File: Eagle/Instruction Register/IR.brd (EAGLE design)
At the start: 160 x 100 mm, 55 parts, among them IC1 SN74HC04N, IC2 SN74HC04N, IC3 SN74HC04N, J1 55959-1630

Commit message: added parts needed to finish boards
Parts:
- added J2: 55959-2430, SamacSys_Parts:559592430
- J1: value 55959-1630 -> 55959-2030; device SamacSys_Parts:SHDR16W65P250X200_2X8_1940X140 -> SamacSys_Parts:55959-2030_1
- moved J1 100.7 mm to (-115.6, -10.2)

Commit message: Finished IR
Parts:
- removed IC3: SN74HC04N, SamacSys_Parts:DIP794W53P254L1930H508Q14N
- moved IC1 244.9 mm to (149.9, 64.8)
- moved CLOCK_GATE 240.9 mm to (110.5, 68.6)
- moved J2 240.0 mm to (80.0, 90.2)
- moved IC2 238.7 mm to (132.1, 64.8)
- moved J1 207.6 mm to (61.0, 99.1)
- moved LEDHLT 186.4 mm to (58.4, 11.4), turned to 270 degrees
- moved RHLT 184.5 mm to (58.4, 20.3), turned to 90 degrees
- moved CONTROL_LOGIC_0-7 181.9 mm to (138.4, 40.6), turned to 90 degrees
- moved CONTROL_LOGIC_16-23 125.5 mm to (64.8, 40.6), turned to 90 degrees
- moved MICROCODE_COUNTER 124.9 mm to (74.9, 67.3)
- moved CONTROL_LOGIC_8-15 124.9 mm to (101.6, 40.6), turned to 90 degrees
- moved IR_OUT_0-7 99.2 mm to (34.3, 80.0)
- moved IR_OUT_8-15 94.4 mm to (16.5, 80.0)
- moved ONE_0-7 89.7 mm to (35.6, 10.2), turned to 90 degrees
- moved ONE_8-15 89.1 mm to (35.6, 22.9), turned to 90 degrees
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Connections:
- removed net N$25: CONTROL_LOGIC_0-7.9
- removed net N$26: CONTROL_LOGIC_0-7.10
- removed net N$27: CONTROL_LOGIC_0-7.11
- removed net N$28: CONTROL_LOGIC_0-7.13
- new net C0: CONTROL_LOGIC_0-7.9, J2.1
- new net C1: CONTROL_LOGIC_0-7.10, J2.3
- new net C2: CONTROL_LOGIC_0-7.11, J2.5
- new net C3: CONTROL_LOGIC_0-7.13, J2.7
- net !ACO: now also J2.11
- net !ALUO: now also J2.15
- net !CO: now also J2.19
- net !IRO: now also J2.14
- net !JMP: now also J2.23
- net !MBRO: now also J2.4
- net !MCR: now also J2.20, MICROCODE_COUNTER.1
- net !ONE: now also J2.12
- net !RI: now also J2.8
- net !RO: now also J2.10
- net !SC: now also J2.9
- net ACI: now also J2.13
- net CE: now also J2.21
- net CLK: now also J1.18
- net GND: now also CLOCK_GATE.10, CLOCK_GATE.12, CLOCK_GATE.13, CLOCK_GATE.4, CLOCK_GATE.5, CLOCK_GATE.9, J1.20
- net HLT: now also J2.24
- net INPUT: now also J2.18
- net IRI: now also J2.16
- net MARI: now also J2.6
- net MBRI: now also J2.2
- net OI: now also J2.22
- net RST: now also J1.17
- net SU: now also J2.17
- net VCC: now also J1.19

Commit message: finished most boards
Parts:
- added C1, C2, C3, C4: (no value), rcl:C025-024X044
- added LED0, LED1, LED10, LED11, LED2, LED3, LED4, LED5, LED6, LED7, LED8, LED9: YELLOW, led:LED3MM
- added LED13, LED14, LED15, LEDACO: BLUE, led:LED3MM
- added R0, R1, R10, R11, R13, R14, R15, R2, R3, R4, R5, R6, R7, R8, R9, RACO: 220, rcl:0204/7
- added U$1, U$2, U$3, U$4: (no value), holes:2,8
- moved LED12 109.2 mm to (24.1, 64.8), turned to 90 degrees
- moved R12 101.7 mm to (24.1, 55.9), turned to 270 degrees
- moved IR_8-15 24.3 mm to (38.1, 49.5), turned to 90 degrees
- moved IR_OUT_0-7 22.9 mm to (57.1, 78.7), turned to 90 degrees
- moved MICROCODE_COUNTER 21.6 mm to (96.5, 68.6)
- moved LEDCE 5.68 mm to (129.5, 14.0)
- moved LEDOI 5.68 mm to (83.8, 14.0)
- moved LEDRI 5.68 mm to (144.8, 14.0)
- moved LEDRO 5.68 mm to (139.7, 14.0)
- moved RCE 5.68 mm to (129.5, 22.9)
- moved ROI 5.68 mm to (83.8, 22.9)
- moved RRI 5.68 mm to (144.8, 22.9)
- moved RRO 5.68 mm to (139.7, 22.9)
- moved LEDACI 5.68 mm to (119.4, 14.0)
- moved LEDALUO 5.68 mm to (99.1, 14.0)
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- renumbered IC1 to NOT_GATE_1, IC2 to NOT_GATE_2, J1 to BUS, J2 to CONTROL_LOGIC
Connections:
- new net N$21: LEDACO.A, RACO.1
- new net N$25: LED1.A, R1.1
- new net N$26: LED2.A, R2.1
- new net N$27: LED3.A, R3.1
- new net N$28: LED4.A, R4.1
- new net N$29: LED5.A, R5.1
- new net N$30: LED6.A, R6.1
- new net N$31: LED7.A, R7.1
- new net N$32: LED8.A, R8.1
- new net N$34: LED9.A, R9.1
- new net N$35: LED10.A, R10.1
- new net N$36: LED11.A, R11.1
- new net N$38: LED13.A, R13.1
- new net N$39: LED14.A, R14.1
- new net N$40: LED15.A, R15.1
- new net N$41: LED0.A, R0.1
- new net N$42: LED0.K, LED1.K, LED10.K, LED11.K, LED12.K, LED13.K, LED14.K, LED15.K, LED2.K, LED3.K, LED4.K, LED5.K, LED6.K, LED7.K, LED8.K, LED9.K
- net ACO: now also RACO.2; no longer R12.2
- net GND: now also C1.1, C2.1, C3.1, C4.1, LEDACO.K; no longer LED12.K
- net IR0: now also R0.2
- net IR1: now also R1.2
- net IR10: now also R10.2
- net IR11: now also R11.2
- net IR12: now also R12.2
- net IR13: now also R13.2
- net IR14: now also R14.2
- net IR15: now also R15.2
- net IR2: now also R2.2
- net IR3: now also R3.2
- net IR4: now also R4.2
- net IR5: now also R5.2
- net IR6: now also R6.2
- net IR7: now also R7.2
- net IR8: now also R8.2
- net IR9: now also R9.2
- net VCC: now also C1.2, C2.2, C3.2, C4.2
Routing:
- net GND: track 0.00 -> 633.3 mm, vias 0 -> 1
- net VCC: track 0.00 -> 472.5 mm, vias 0 -> 4
- net !ONE: track 0.00 -> 246.0 mm, vias 0 -> 1
- net IR14: track 0.00 -> 211.5 mm, vias 0 -> 3
- net IR13: track 0.00 -> 201.1 mm, vias 0 -> 2
- net B10: track 0.00 -> 200.9 mm, vias 0 -> 2
- net B5: track 0.00 -> 197.9 mm
- net INPUT: track 0.00 -> 193.4 mm, vias 0 -> 2
- net IR15: track 0.00 -> 190.8 mm, vias 0 -> 4
- net CE: track 0.00 -> 180.7 mm
- net !IRO: track 0.00 -> 173.8 mm, vias 0 -> 4
- net B4: track 0.00 -> 172.3 mm
- net MARI: track 0.00 -> 161.3 mm, vias 0 -> 2
- net IRI: track 0.00 -> 161.3 mm, vias 0 -> 2
- net IR12: track 0.00 -> 160.3 mm, vias 0 -> 5
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
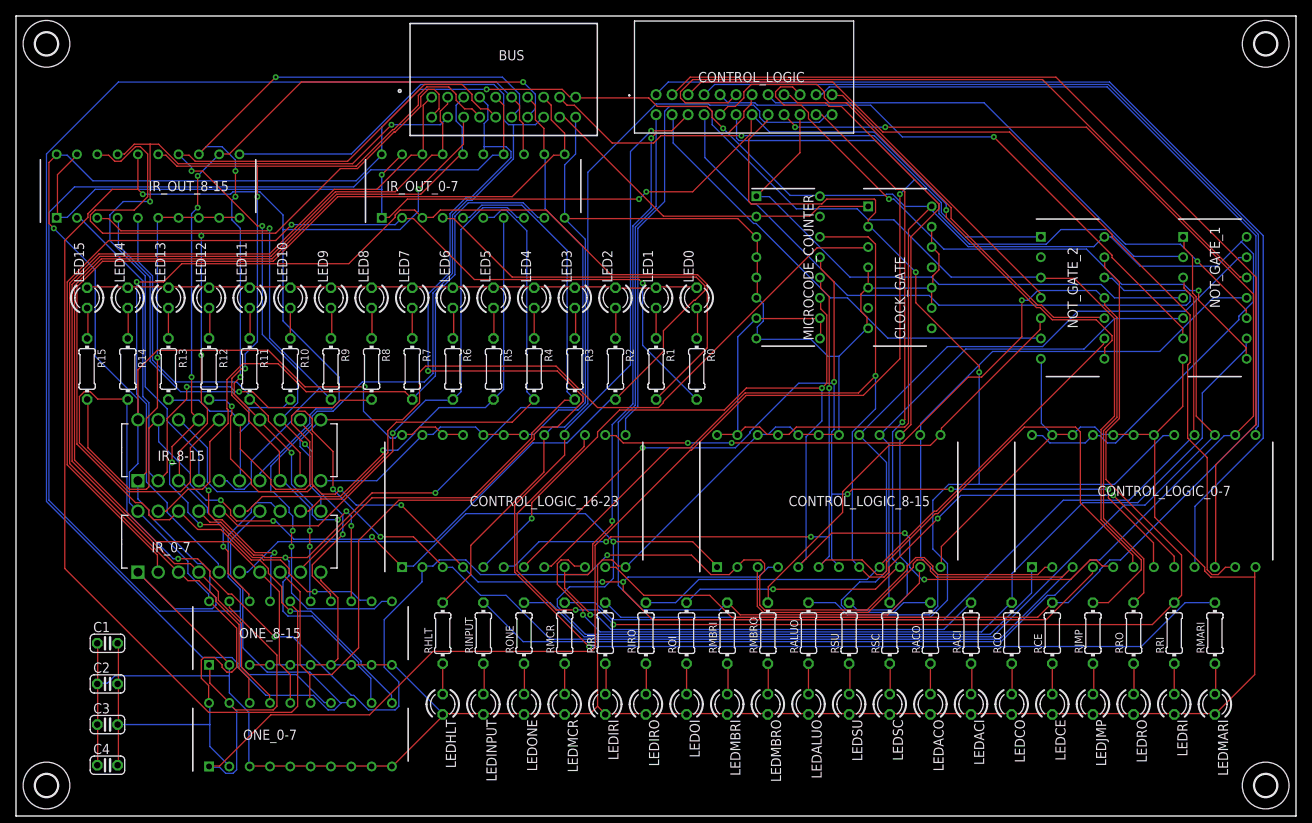
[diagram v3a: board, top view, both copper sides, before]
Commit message: added Clock
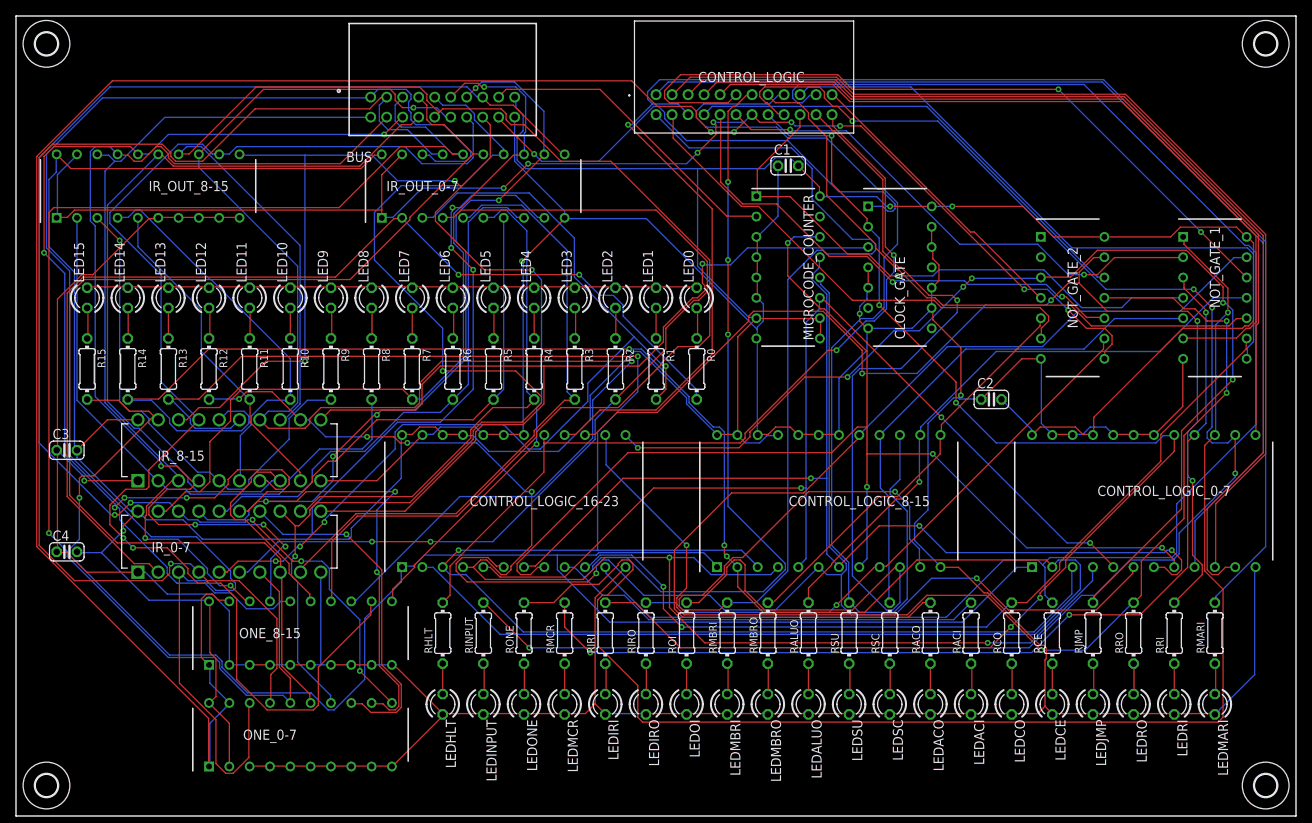
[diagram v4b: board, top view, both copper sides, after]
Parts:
- moved C2 116.1 mm to (121.9, 52.1)
- moved C1 103.9 mm to (96.5, 81.3)
- moved C3 34.7 mm to (6.35, 45.7)
- moved C4 27.1 mm to (6.35, 33.0)
- moved BUS 7.62 mm to (53.3, 99.1)
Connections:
- new net !CLK: BUS.17, MICROCODE_COUNTER.2
- net CLK: no longer MICROCODE_COUNTER.2
- net RST: no longer BUS.17
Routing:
- net B12: track 116.1 -> 200.0 mm, vias 4 -> 0
- net B5: track 197.9 -> 126.8 mm, vias 0 -> 5
- net RST: track 68.9 -> 0.00 mm, vias 1 -> 0
- net B0: track 121.2 -> 182.8 mm
- net B13: track 119.8 -> 181.0 mm, vias 8 -> 2
- net ONE: track 125.1 -> 177.8 mm, vias 0 -> 1
- net IR14: track 211.5 -> 263.9 mm
- net B10: track 200.9 -> 154.2 mm, vias 2 -> 5
- net SU: track 84.9 -> 127.7 mm
- net MBRI: track 104.5 -> 146.9 mm, vias 0 -> 1
- net B14: track 124.1 -> 164.1 mm, vias 7 -> 2
- net MARI: track 161.3 -> 200.7 mm, vias 2 -> 1
- net !CLK: track 0.00 -> 39.2 mm
- net B4: track 172.3 -> 134.6 mm, vias 0 -> 2
- net B2: track 132.0 -> 166.9 mm, vias 0 -> 1
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
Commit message: added gerber files for each board
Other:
- board text added: "MARIE PC Instruction Register Architecture design by: Dr. Linda Null Hardware implementation by: Richard Bowser"
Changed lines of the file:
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@@
 <drawing>
 <settings>
-<setting alwaysvectorfont="no"/>
+<setting alwaysvectorfont="yes"/>
 <setting verticaltext="up"/>
 </settings>
@@
 <wire x1="160" y1="100" x2="0" y2="100" width="0" layer="20"/>
 <wire x1="0" y1="100" x2="0" y2="0" width="0" layer="20"/>
+<text x="151.13" y="81.28" size="1.778" layer="26" rot="MR0">MARIE PC
+Instruction Register
+Architecture design by: Dr. Linda Null
+Hardware implementation by: Richard Bowser</text>
 </plain>
 <attributes>
@@
 </drawing>
 <compatibility>
+<note version="6.3" minversion="6.2.2" severity="warning">
+Since Version 6.2.2 text objects can contain more than one line,
+which will not be processed correctly with this version.
+</note>
 <note version="8.2" severity="warning">
 Since Version 8.2, EAGLE supports online libraries. The ids

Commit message: added gerber files for ordering boards
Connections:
- removed net !RST: NOT_GATE_2.2
- removed net RST: NOT_GATE_2.1
- net VCC: now also NOT_GATE_2.1
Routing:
- net IR14: track 263.9 -> 199.9 mm, vias 3 -> 4
- net !IRO: track 171.8 -> 223.3 mm, vias 8 -> 1
- net B14: track 164.1 -> 211.9 mm
- net ONE: track 177.8 -> 132.9 mm, vias 1 -> 3
- net GND: track 614.4 -> 658.0 mm, vias 4 -> 2
- net RO: track 146.6 -> 107.0 mm, vias 4 -> 5
- net B1: track 157.0 -> 120.2 mm, vias 1 -> 4
- net ACO: track 127.4 -> 91.5 mm, vias 0 -> 1
- net IRI: track 165.3 -> 134.9 mm, vias 5 -> 3
- net B0: track 182.8 -> 154.8 mm, vias 0 -> 2
- net MBRI: track 146.9 -> 119.4 mm, vias 1 -> 0
- net VCC: track 463.0 -> 436.2 mm
- net B2: track 166.9 -> 140.8 mm, vias 1 -> 0
- net JMP: track 135.3 -> 111.7 mm, vias 6 -> 4
- net N$1: track 150.1 -> 127.7 mm
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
